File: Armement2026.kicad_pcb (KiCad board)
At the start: 2 copper layers, 87.5 x 61.5 mm, 24 parts, among them J1 Screw_Terminal_01x02, J10 Screw_Terminal_01x02, J11 Screw_Terminal_01x02, J12 Screw_Terminal_01x02, J2 Screw_Terminal_01x02, J5 Screw_Terminal_01x02, J6 Screw_Terminal_01x02, J8 Screw_Terminal_01x02, J9 Screw_Terminal_01x02, Q1 NTR4101PT1G, Q2 NTR4101PT1G, SW1 SW_Nidec_CAS-120A1, SW2 SW_Nidec_CAS-120A1, SW3 SW_Nidec_CAS-120A1, U1 LDO_4v2-MIC5209-4.2YS-TR

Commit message: PCB Armement IRECxFAR-OUT
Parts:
- removed F1: Polyfuse, Fuse:Fuse_1812_4532Metric
- removed J10: Screw_Terminal_01x02, Connector_PinHeader_2.54mm:PinHeader_1x02_P2.54mm_Vertical
- removed J12: Screw_Terminal_01x02, Connector_Molex:Molex_Micro-Fit_3.0_43650-0215_1x02_P3.00mm_Vertical
- removed J9: Screw_Terminal_01x02, Connector_PinHeader_1.27mm:PinHeader_1x02_P1.27mm_Vertical
- added J3: Screw_Terminal_01x02, Connector_AMASS:AMASS_XT30U-M_1x02_P5.0mm_Vertical, F.Cu at (113.0, 104.5)
- added J4: Screw_Terminal_01x02, Connector_AMASS:AMASS_XT30U-M_1x02_P5.0mm_Vertical, F.Cu at (70.2, 105.3)
- added J7: Screw_Terminal_01x02, Connector_JST:JST_SH_BM02B-SRSS-TB_1x02-1MP_P1.00mm_Vertical, F.Cu at (102.8, 104.4)
- added JP1: SolderJumper_2_Open, Jumper:SolderJumper-2_P1.3mm_Open_TrianglePad1.0x1.5mm, F.Cu at (124.0, 137.4)
- added JP2: SolderJumper_2_Open, Jumper:SolderJumper-2_P1.3mm_Open_TrianglePad1.0x1.5mm, F.Cu at (86.0, 111.7)
- added JP3: SolderJumper_2_Open, Jumper:SolderJumper-2_P1.3mm_Open_TrianglePad1.0x1.5mm, F.Cu at (102.6, 111.7)
- added JP4: SolderJumper_2_Open, Jumper:SolderJumper-2_P1.3mm_Open_TrianglePad1.0x1.5mm, F.Cu at (107.3, 111.8)
- added JP5: SolderJumper_2_Open, Jumper:SolderJumper-2_P1.3mm_Open_TrianglePad1.0x1.5mm, F.Cu at (93.5, 111.7)
- J2: footprint footprints:CONN_70545-xxxx_02_MOL -> Connector_Molex:Molex_Micro-Fit_3.0_43650-0215_1x02_P3.00mm_Vertical
- J5: footprint 3mm header 2x1:CONN_SD-44067-001_02_MOL -> Connector_AMASS:AMASS_XT30U-M_1x02_P5.0mm_Vertical
- J6: footprint footprints:CONN_SDA_43255-00XX_02_MOL -> footprints:CONN_70545-xxxx_02_MOL
- J8: footprint footprints:CONN02_560020_MOL -> Connector_JST:JST_PH_B2B-PH-K_1x02_P2.00mm_Vertical
- moved J6 75.9 mm to (136.6, 133.2), turned to -90 degrees
- moved J2 34.8 mm to (128.6, 134.7), turned to 90 degrees
- moved J8 17.6 mm to (122.3, 111.4), turned to 180 degrees
- moved J5 7.66 mm to (95.0, 106.3), turned to 180 degrees
- moved C1 6.44 mm to (141.0, 120.0)
- moved C2 6.31 mm to (129.6, 109.0)
- moved U1 6.31 mm to (134.2, 118.4)
- moved J11 2.22 mm to (78.7, 105.3)
- moved DZ1 1.40 mm to (66.8, 127.0)
- moved Q1 0.99 mm to (71.7, 129.6), turned to -90 degrees
- moved Q2 0.56 mm to (125.4, 145.7), turned to 0 degrees
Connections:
- C2 pad 1: Net-(J12-Pin_1) -> Net-(J8-Pin_1)
- C7 pad 2: Net-(J10-Pin_1) -> Net-(J2-Pin_2)
- DZ1 pad 1: Net-(DZ1-K) -> 7v4
- J1 pad 1: GND -> Net-(J1-Pin_1)
- J2 pad 1: Net-(J2-Pin_1) -> Net-(DZ2-K)
- J5 pad 1: 7v4 -> GND
- J5 pad 2: GND -> Net-(J5-Pin_2)
- J6 pad 1: 7v4 -> Net-(J2-Pin_2)
- J6 pad 2: GND -> Net-(J6-Pin_2)
- J8 pad 1: 7v4 -> Net-(J8-Pin_1)
- PWR_R2 pad 2: Net-(J10-Pin_1) -> Net-(J2-Pin_2)
- Q1 pad 1: GND -> Net-(Q1-D)
- Q1 pad 3: Net-(DZ1-K) -> 7v4
- SW1 pad 1: GND -> Net-(J1-Pin_1)
- SW1 pad 2: GND -> Net-(Q1-D)
- SW2 pad 1: Net-(J2-Pin_1) -> Net-(J7-Pin_1)
- SW2 pad 2: Net-(J2-Pin_2) -> Net-(JP3-A)
- SW3 pad 2: Net-(J10-Pin_2) -> Net-(J6-Pin_2)
- U1 pad 3: Net-(J12-Pin_1) -> Net-(J8-Pin_1)
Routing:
- net Net-(J7-Pin_1): track 0.00 -> 48.6 mm
- net Net-(J2-Pin_1): track 38.3 -> 0.00 mm
- net GND: track 101.7 -> 64.1 mm
- net Net-(JP3-A): track 0.00 -> 31.7 mm
- net Net-(J6-Pin_2): track 0.00 -> 27.7 mm
- net Net-(J10-Pin_2): track 21.9 -> 0.00 mm
- net Net-(J8-Pin_1): track 0.00 -> 20.5 mm
- net Net-(J12-Pin_1): track 19.5 -> 0.00 mm
- net Net-(J10-Pin_1): track 18.9 -> 0.00 mm
- net Net-(J1-Pin_1): track 0.00 -> 14.8 mm
- net Net-(Q1-D): track 0.00 -> 14.5 mm
- net Net-(J5-Pin_2): track 0.00 -> 13.4 mm
- net Net-(JP1-B): track 10.5 -> 18.3 mm
- net Net-(DZ1-K): track 7.56 -> 0.00 mm
- net Net-(J7-Pin_2): track 0.00 -> 6.69 mm
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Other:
- outline, holes or cut-outs redrawn
- board text added: "1"
- board text added: "2"
- board text added: "7v4 17mAh"
- board text added: "7v4 4.2mAh"
- board text added: "Altimeter"
- board text added: "Feather"
- board text added: "ODB"
- board text added: "Option 1: Solder this option to use the ODB as the third flight computer. Option 2: Solder this option to use the ODB as the second flight computer (without the Stratologger)."
- board text added: "PCB Armement 2026 IREC + Far-Out Alexis Giroux"
- board text added: "Strato"

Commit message: commit
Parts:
- added J10: Screw_Terminal_01x02, TerminalBlock:TerminalBlock_MaiXu_MX126-5.0-02P_1x02_P5.00mm, F.Cu at (100.7, 89.9)
- added J9: Screw_Terminal_01x02, RCJ_054:CUI_RCJ-054, F.Cu at (131.9, 101.2)
- added SW4: SW_Nidec_CAS-120A1, Library:Omrun_SS-01GL13, F.Cu at (114.2, 104.2)
- moved J3 20.7 mm to (126.7, 88.9), turned to 0 degrees
- moved J5 11.5 mm to (83.5, 105.3)
- moved J4 11.1 mm to (61.1, 111.8)
- moved J8 10.0 mm to (132.3, 111.2)
- moved J11 8.60 mm to (70.0, 105.2)
- moved JP2 8.50 mm to (77.5, 111.6)
- moved JP5 8.50 mm to (85.0, 111.6)
- moved C2 8.31 mm to (137.4, 111.8), turned to 90 degrees
- moved J7 6.60 mm to (96.2, 104.2)
- moved JP3 6.60 mm to (96.0, 111.5)
- moved JP4 6.60 mm to (100.7, 111.5)
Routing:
- net Net-(J10-Pin_1): track 0.00 -> 32.7 mm
- net Net-(J9-Pin_1): track 0.00 -> 24.3 mm
- net Net-(J10-Pin_2): track 0.00 -> 23.7 mm
- net Net-(J8-Pin_1): track 20.5 -> 8.85 mm
- net GND: track 64.1 -> 59.3 mm
- net Net-(JP3-A): track 31.7 -> 35.8 mm
- net Net-(J7-Pin_1): track 48.6 -> 52.4 mm
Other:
- board size 87.5 x 61.5 mm -> 87.5 x 77.5 mm
- board text added: "3rd"
- board text added: "Motor Igniter"

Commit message: wtf did I just do
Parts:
- added G***: LOGO, LOGO, F.Cu at (100.2, 157.6)
- added J12: Screw_Terminal_01x02, TerminalBlock:TerminalBlock_MaiXu_MX126-5.0-02P_1x02_P5.00mm, F.Cu at (133.3, 102.9)
- added JP6: SolderJumper_2_Open, Jumper:SolderJumper-2_P1.3mm_Open_TrianglePad1.0x1.5mm, F.Cu at (86.2, 107.7)
- J2: footprint Connector_Molex:Molex_Micro-Fit_3.0_43650-0215_1x02_P3.00mm_Vertical -> 3mm header 2x1:CONN_SD-44067-001_02_MOL
- J7: footprint Connector_JST:JST_SH_BM02B-SRSS-TB_1x02-1MP_P1.00mm_Vertical -> Connector_PinHeader_2.54mm:PinHeader_1x02_P2.54mm_Vertical
- J9: footprint RCJ_054:CUI_RCJ-054 -> Connector_JST:JST_SH_BM02B-SRSS-TB_1x02-1MP_P1.00mm_Vertical
- Q1, Q2: value NTR4101PT1G -> DMP10H400SK3-13; footprint NTR4101PT1G:SOT-23-3_1P4X3P040_ONS -> footprints3:TO252-DPAK-DMP10H400SK3_DIO
- moved J4 71.4 mm to (132.4, 114.3), turned to 0 degrees
- moved C1 45.2 mm to (100.0, 101.0), turned to 0 degrees
- moved C2 43.5 mm to (94.7, 104.2), turned to 180 degrees
- moved J8 38.2 mm to (94.2, 109.3), turned to -90 degrees
- moved U1 34.7 mm to (101.3, 107.4), turned to 180 degrees
- moved J5 26.0 mm to (60.9, 118.1), turned to 90 degrees
- moved JP4 24.1 mm to (124.7, 113.6), turned to 0 degrees
- moved JP2 21.7 mm to (94.8, 98.6), turned to 90 degrees
- moved JP5 20.9 mm to (105.8, 112.6), turned to -90 degrees
- moved C8 18.9 mm to (62.2, 138.2), turned to 0 degrees
- moved J7 18.0 mm to (78.5, 107.4)
- moved JP1 12.6 mm to (133.7, 145.5)
- moved JP3 12.5 mm to (85.9, 104.0), turned to 0 degrees
- moved PWR_R2 11.2 mm to (133.2, 136.7)
- moved J9 9.81 mm to (125.9, 109.0)
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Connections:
- C1 pad 1: 7v4 -> Net-(JP2-A)
- J5 pad 2: Net-(J5-Pin_2) -> 7v4
- J6 pad 1: Net-(J2-Pin_2) -> Net-(J6-Pin_1)
- J6 pad 2: Net-(J6-Pin_2) -> Net-(J2-Pin_2)
- J9 pad 2: Net-(J10-Pin_1) -> Net-(J12-Pin_1)
- JP2 pad 1: Net-(J5-Pin_2) -> Net-(JP2-A)
- JP3 pad 1: Net-(JP3-A) -> Net-(J7-Pin_1)
- JP3 pad 2: 7v4 -> Net-(J8-Pin_1)
- JP4 pad 1: Net-(JP3-A) -> Net-(J10-Pin_2)
- JP4 pad 2: Net-(J7-Pin_2) -> Net-(J9-Pin_1)
- JP5 pad 1: Net-(J7-Pin_1) -> GND
- JP5 pad 2: Net-(J5-Pin_2) -> Net-(JP5-B)
- SW2 pad 1: Net-(J7-Pin_1) -> Net-(JP5-B)
- SW2 pad 2: Net-(JP3-A) -> Net-(J7-Pin_2)
- SW3 pad 2: Net-(J6-Pin_2) -> Net-(J6-Pin_1)
- SW4 pad 2: Net-(J9-Pin_1) -> Net-(J12-Pin_1)
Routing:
- net Net-(JP5-B): track 0.00 -> 58.6 mm
- net Net-(J7-Pin_1): track 52.4 -> 11.3 mm
- net Net-(JP3-A): track 35.8 -> 0.00 mm
- net Net-(J6-Pin_1): track 0.00 -> 34.4 mm
- net Net-(J7-Pin_2): track 6.69 -> 38.3 mm
- net Net-(J12-Pin_1): track 0.00 -> 28.0 mm
- net Net-(J6-Pin_2): track 27.7 -> 0.00 mm
- net Net-(J9-Pin_1): track 24.3 -> 4.78 mm
- net Net-(J5-Pin_2): track 13.7 -> 0.00 mm
- net Net-(J10-Pin_2): track 23.7 -> 35.8 mm
- net Net-(J8-Pin_1): track 8.85 -> 20.9 mm
- net GND: track 59.3 -> 51.3 mm, vias 0 -> 9
- net Net-(DZ1-A): track 12.0 -> 5.93 mm
- net Net-(JP2-A): track 0.00 -> 4.31 mm
- net Net-(JP1-B): track 18.3 -> 22.0 mm
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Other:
- board size 87.5 x 77.5 mm -> 87.5 x 77.6 mm
- board text added: "3"
- board text added: "Battery Feather"
- board text added: "Pmos"
- board text added: "System"
- board text removed: "Option 1: Solder this option to use the ODB as the third flight computer. Option 2: Solder this option to use the ODB as the second flight computer (without the Stratologger)."
- board text removed: "Strato"

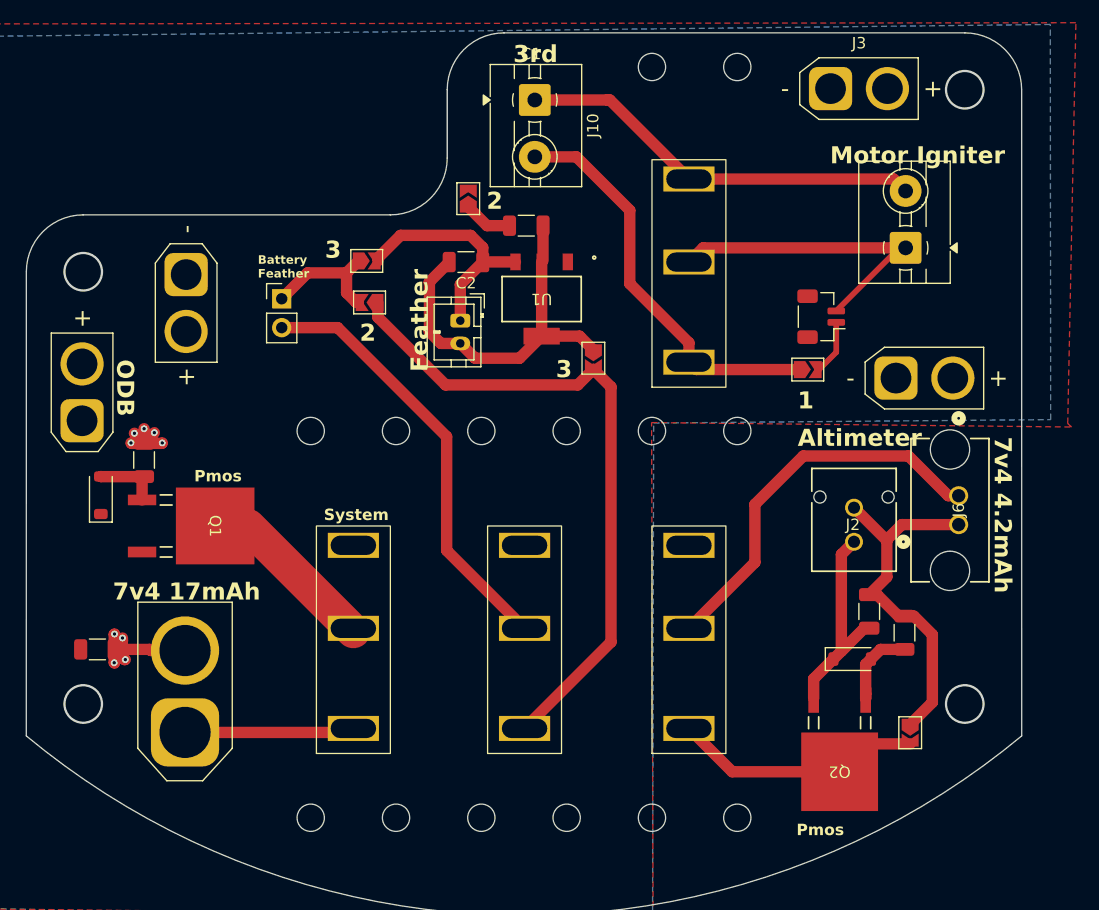
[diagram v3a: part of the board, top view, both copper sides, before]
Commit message: commande PCB armement
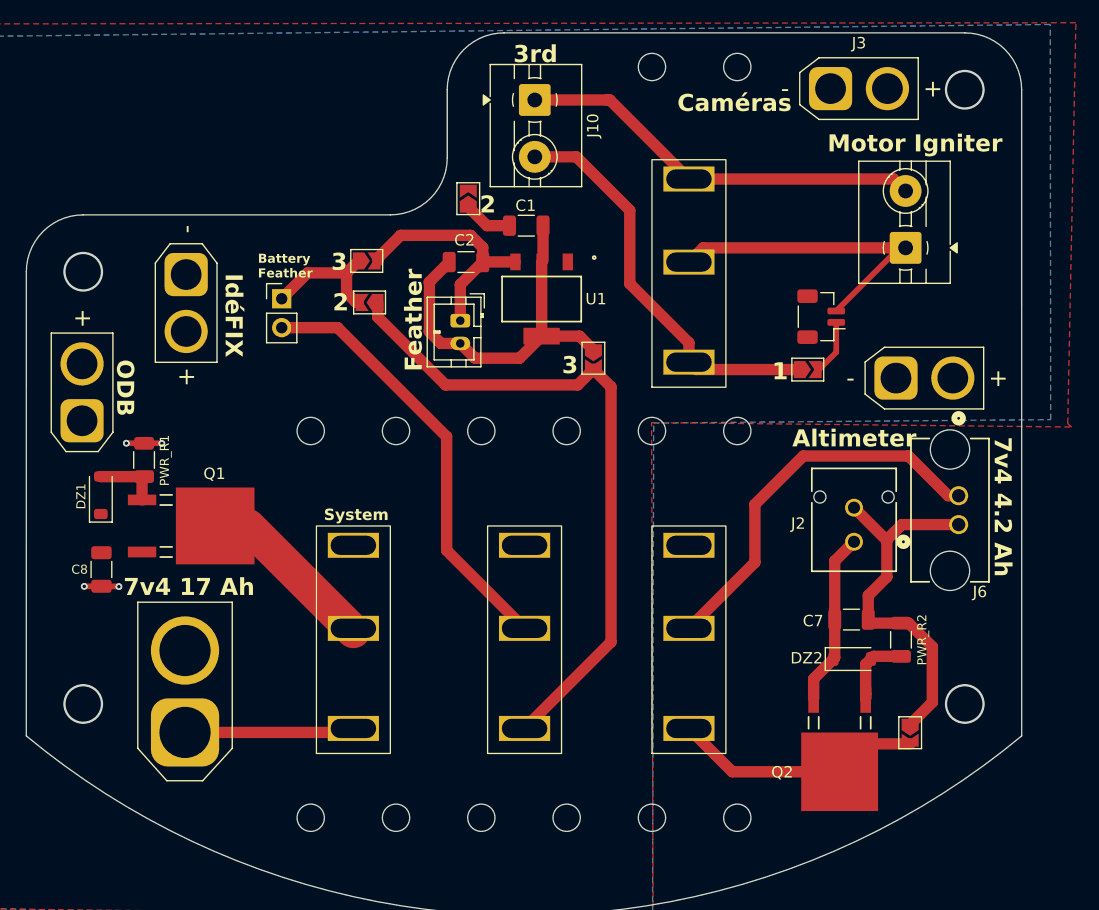
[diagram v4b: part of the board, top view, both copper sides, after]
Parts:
- G***: moved to B.Cu
- moved C8 7.04 mm to (62.6, 131.2), turned to -90 degrees
- moved C7 1.72 mm to (128.5, 135.6), turned to 0 degrees
- moved PWR_R2 0.69 mm to (132.9, 137.4)
- moved G*** 0.40 mm to (99.8, 157.8), turned to 180 degrees
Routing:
- net GND: track 51.3 -> 39.4 mm, vias 9 -> 4
- net Net-(DZ2-K): track 19.5 -> 15.5 mm
- net Net-(J2-Pin_2): track 32.3 -> 33.0 mm
- net Net-(DZ2-A): track 7.89 -> 7.34 mm
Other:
- board text added: "7v4 17 Ah"
- board text added: "7v4 4.2 Ah"
- board text added: "Caméras"
- board text added: "IdéFIX"
- board text removed: "7v4 17mAh"
- board text removed: "7v4 4.2mAh"
- board text removed: "Pmos"
